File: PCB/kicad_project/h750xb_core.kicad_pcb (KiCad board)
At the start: 4 copper layers, 50 x 50 mm, 99 parts, among them Q1 Q_NMOS_GSD, SW1 SW_DPST, SW2 SW_DPST, U1 STM32H750XBHx, U2 TPS74801DRC, U3 TPS82130, U4 REF3020, U5 IS42S16160J, U6 IS42S16160J, U7 W25Q32JVZP, U8 W25Q32JVZP, Y1 32M, Y2 32.768k

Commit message: 123
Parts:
- moved D3 27.9 mm to (3.37, 92.2)
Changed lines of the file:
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@@
 	(footprint "Package_TO_SOT_SMD:SOT-23"
 		(layer "F.Cu")
-		(at -23.495 84.582)
+		(at 3.3704 92.248)
 		(descr "SOT, 3 Pin (https://www.jedec.org/system/files/docs/to-236h.pdf variant AB), generated with kicad-footprint-generator ipc_gullwing_generator.py")
 		(tags "SOT TO_SOT_SMD")
@@
 		(tags "resistor")
 		(property "Reference" "R8"
-			(at 0 -1.17 360)
+			(at 0 -1.17 0)
 			(layer "F.SilkS")
 			(hide yes)
@@
 		)
 		(property "Value" "4.99kΩ/12kΩ"
-			(at 0 1.17 360)
+			(at 0 1.17 0)
 			(layer "F.Fab")
 			(hide yes)
@@
 		)
 		(fp_text user "${REFERENCE}"
-			(at 0 0 360)
+			(at 0 0 0)
 			(layer "F.Fab")
 			(effects
@@
 		(tags "capacitor")
 		(property "Reference" "C42"
-			(at 0 -1.16 270)
+			(at 0 -1.16 -90)
 			(layer "F.SilkS")
 			(hide yes)
@@
 		)
 		(property "Value" "4.7uF"
-			(at 0 1.16 270)
+			(at 0 1.16 -90)
 			(layer "F.Fab")
 			(hide yes)
@@
 		)
 		(fp_text user "${REFERENCE}"
-			(at 0 0 270)
+			(at 0 0 -90)
 			(layer "F.Fab")
 			(effects

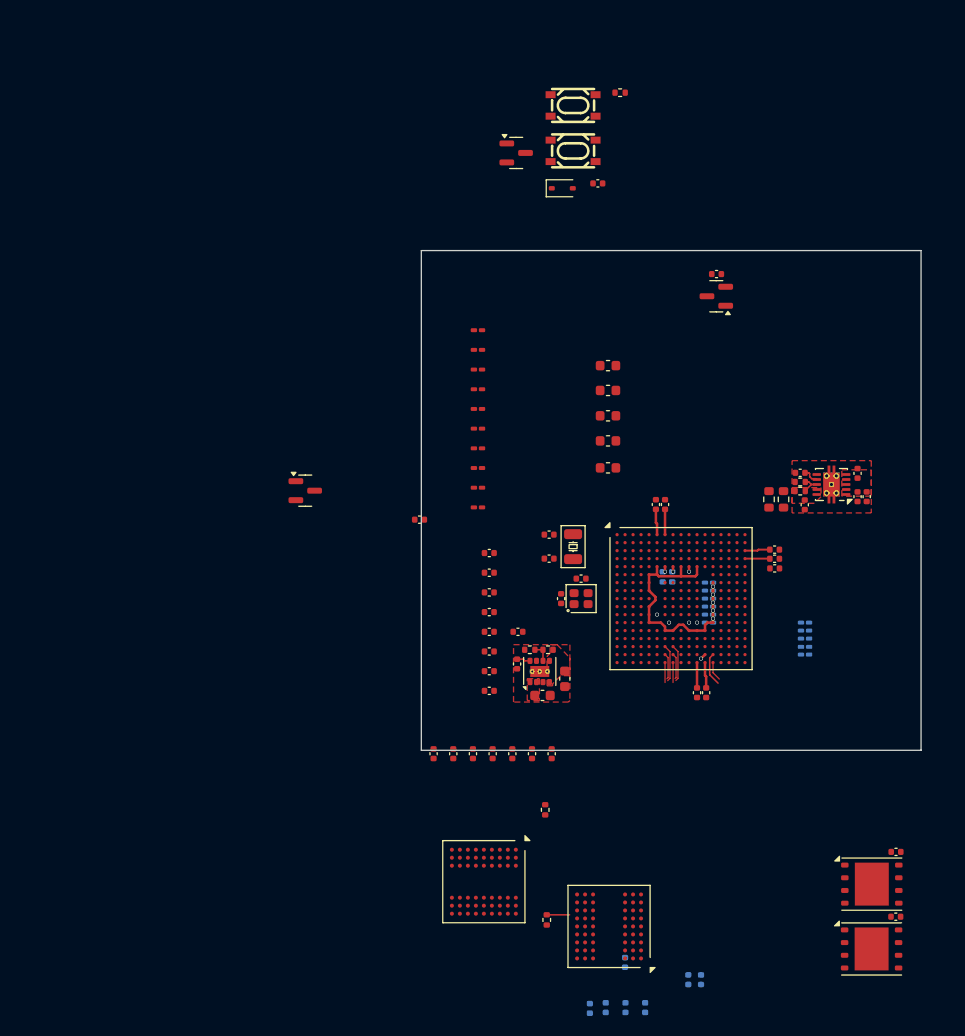
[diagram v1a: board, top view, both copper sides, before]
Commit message: 更新物料 删除16bit sdram*2 改为32bit sdram*1
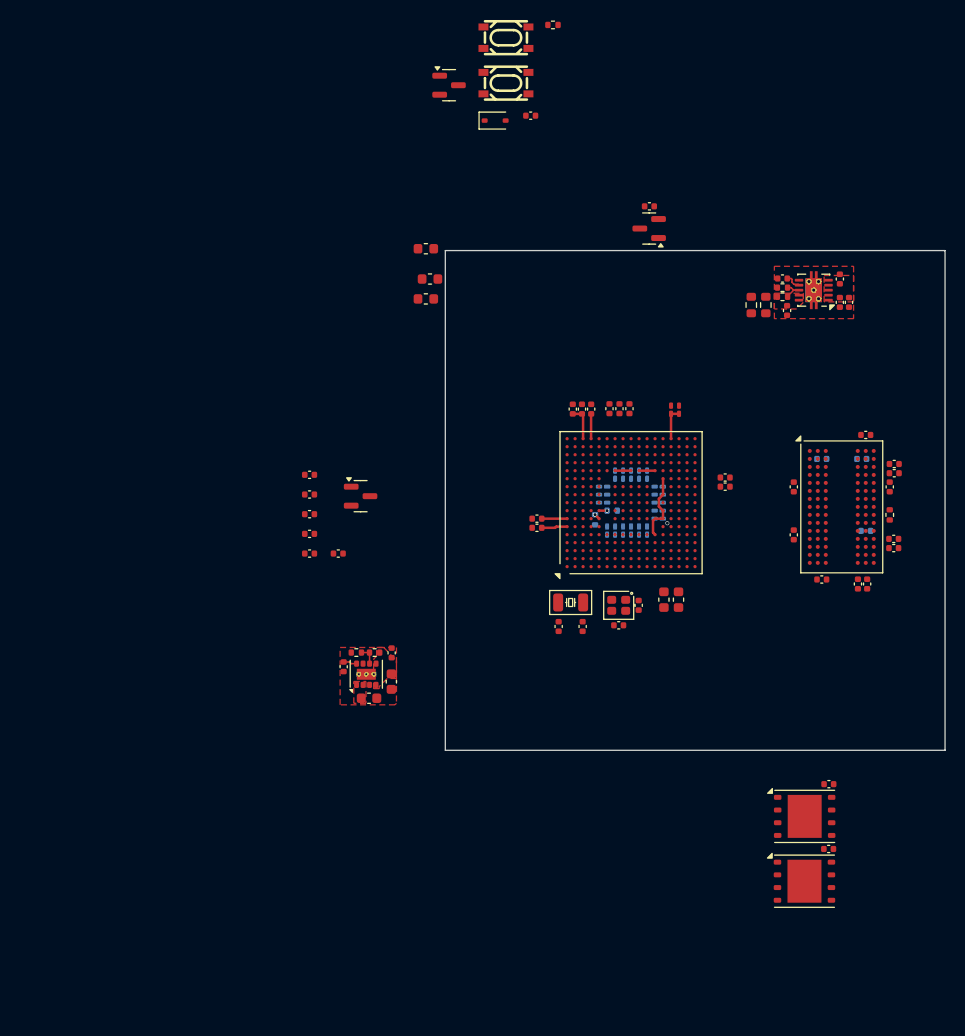
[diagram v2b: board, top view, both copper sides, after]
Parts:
- removed R12: 10K, Resistor_SMD:R_0402_1005Metric
- removed U5, U6: IS42S16160J, Package_BGA:Alliance_TFBGA-54_8x8mm_Layout9x9_P0.8mm
- added U9: ~, Package_BGA:BGA-90_8.0x13.0mm_Layout2x3x15_P0.8mm, F.Cu at (57.1, 93.9)
- C1, C10, C3, C4, C5, C6, C7, C8, C9: moved to B.Cu
- C16, C47, C48, C50, C53: moved to F.Cu
- R9: value 100kΩ -> 309kΩ
- moved C47 63.7 mm to (59.5, 86.7), turned to 180 degrees
- moved C48 57.6 mm to (61.9, 91.9), turned to -90 degrees
- moved C53 55.9 mm to (62.3, 90.5), turned to 180 degrees
- moved C52 54.9 mm to (59.1, 89.1), turned to 180 degrees
- moved C51 53.5 mm to (55.1, 89.1), turned to 180 degrees
- moved C49 53.4 mm to (59.5, 96.3), turned to 180 degrees
- moved R5 53.1 mm to (61.9, 94.7)
- moved C50 49.3 mm to (58.7, 101.6)
- moved C58 46.9 mm to (62.3, 98.0), turned to 180 degrees
- moved C60 46.6 mm to (59.6, 101.6), turned to 90 degrees
- moved C54 44.9 mm to (62.3, 89.6), turned to 180 degrees
- moved C56 43.8 mm to (62.3, 97.1), turned to 180 degrees
- moved C59 40.8 mm to (55.1, 101.1), turned to 180 degrees
- moved C55 37.4 mm to (52.3, 91.9), turned to 90 degrees
- moved C57 37.2 mm to (52.3, 96.7), turned to 90 degrees
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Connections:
- C27 pad 1: Net-(U1-VDD33_USB) -> +3V3
- C28 pad 1: Net-(U1-VDD33_USB) -> +3V3
- C29 pad 1: Net-(U1-VDD33_USB) -> +3V3
- U1 pad F17: Net-(U1-VDD33_USB) -> +3V3
- U1 pad G17: Net-(U1-VDD33_USB) -> +3V3
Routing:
- net +3V3: track 24.9 -> 13.4 mm, vias 5 -> 0
- net GND: track 4.25 -> 0.00 mm, vias 5 -> 0
- net /mcu/SDRAM_A6: track 3.71 -> 0.00 mm
- net /mcu/SDRAM_D16: track 3.34 -> 0.00 mm
- net /mcu/SDRAM_RAS: track 2.59 -> 0.00 mm
- net /mcu/SDRAM_A10: track 2.57 -> 0.00 mm
- net /mcu/VCAP: track 7.56 -> 5.02 mm
- net /mcu/SDRAM_CS#: track 2.29 -> 0.00 mm
- net unconnected-(U1-PJ4-PadU7): track 2.00 -> 0.00 mm
- net /mcu/SDRAM_A11: track 2.00 -> 0.00 mm
- net unconnected-(U1-PH7-PadU13): track 1.91 -> 0.00 mm
- net /mcu/VDDLDO: track 8.16 -> 6.36 mm
- net unconnected-(U1-PJ13-PadE10): track 0.51 -> 0.00 mm, vias 1 -> 0
- net unconnected-(U1-PJ0-PadN6): vias 0 -> 1

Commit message: MCU部分扇出，SDRAM走线ing
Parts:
- C22, C23, C24: moved to B.Cu
- C49, C51, C52, R2: moved to F.Cu
- moved FB2 45.7 mm to (43.2, 104.3), turned to -90 degrees
- moved U8 44.5 mm to (21.3, 100.4)
- moved U7 44.1 mm to (21.3, 94.5)
- moved C64 42.5 mm to (25.2, 98.5), turned to -90 degrees
- moved C63 42.1 mm to (25.2, 92.6), turned to -90 degrees
- moved C23 37.6 mm to (40.2, 102.2)
- moved C24 37.0 mm to (40.2, 101.3)
- moved C22 35.9 mm to (37.8, 102.2), turned to -90 degrees
- moved R2 6.13 mm to (28.0, 94.2), turned to 180 degrees
- moved C51 4.94 mm to (50.2, 89.8), turned to 90 degrees
- moved C65 2.75 mm to (30.2, 103.5), turned to 180 degrees
- moved C66 2.75 mm to (32.6, 103.5), turned to 0 degrees
- moved Y2 2.52 mm to (31.4, 105.5)
- moved R1 2.22 mm to (34.6, 95.4), turned to 0 degrees
- moved C53 2.12 mm to (60.2, 90.9)
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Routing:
- net /mcu/SDRAM_DQM2: track 0.00 -> 35.1 mm, vias 0 -> 1
- net +3V3: track 13.4 -> 47.7 mm, vias 0 -> 18
- net /mcu/SDRAM_DQM1: track 0.00 -> 33.2 mm, vias 0 -> 1
- net /mcu/SDRAM_D29: track 0.00 -> 33.0 mm, vias 0 -> 1
- net /mcu/SDRAM_DQM3: track 0.00 -> 32.1 mm, vias 0 -> 1
- net /mcu/SDRAM_CAS: track 0.00 -> 31.8 mm, vias 0 -> 1
- net /mcu/SDRAM_A0: track 0.00 -> 30.8 mm, vias 0 -> 1
- net /mcu/SDRAM_DQM0: track 0.00 -> 29.9 mm, vias 0 -> 2
- net /mcu/SDRAM_D24: track 0.00 -> 28.8 mm, vias 0 -> 1
- net /mcu/SDRAM_D28: track 0.00 -> 28.6 mm, vias 0 -> 1
- net /mcu/SDRAM_A1: track 0.00 -> 28.3 mm, vias 0 -> 1
- net /mcu/SDRAM_D30: track 0.00 -> 27.1 mm, vias 0 -> 2
- net /mcu/SDRAM_D26: track 0.00 -> 26.8 mm, vias 0 -> 1
- net /mcu/SDRAM_D2: track 0.00 -> 26.7 mm, vias 0 -> 2
- net /mcu/SDRAM_D27: track 0.00 -> 26.6 mm, vias 0 -> 1
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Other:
- copper layers 4 -> 6

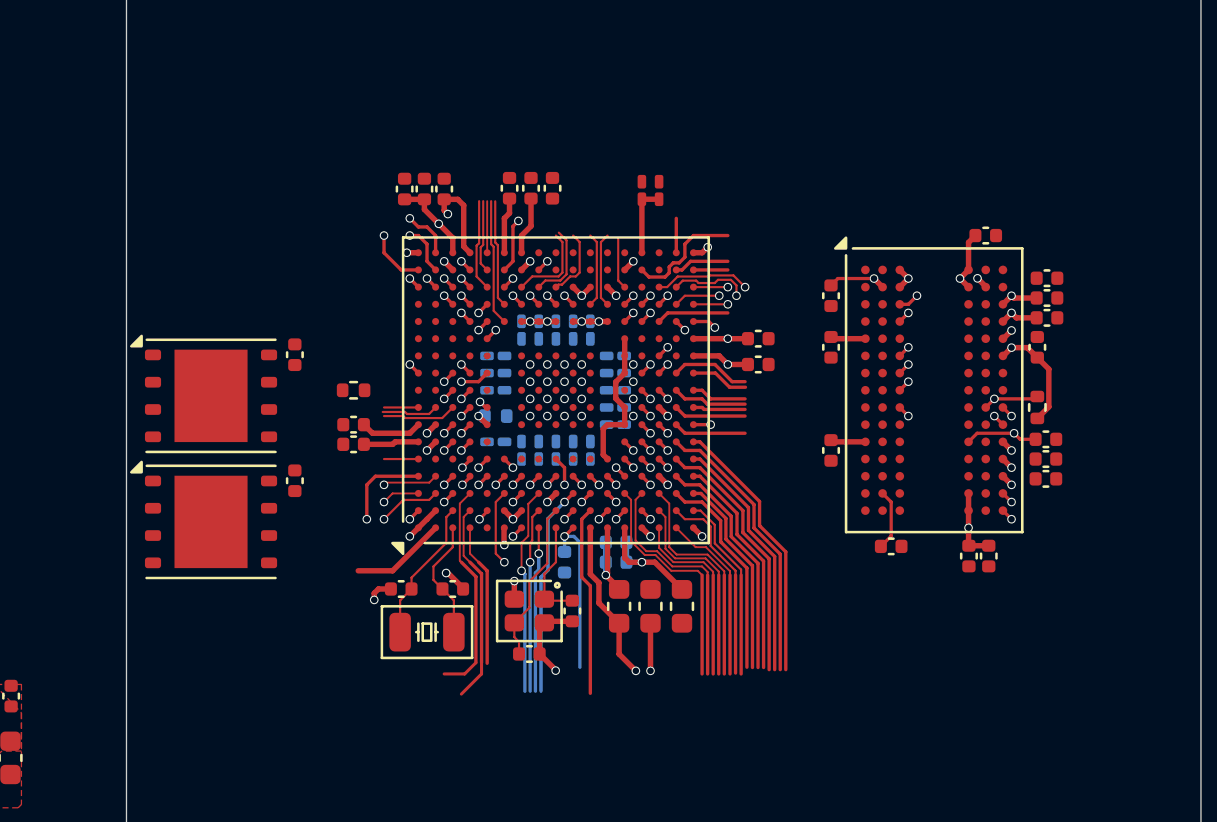
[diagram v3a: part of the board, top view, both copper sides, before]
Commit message: 绕走SDRAM走线。。因复杂度太高，放弃做等长 目前差最后几根数据线，可视情况交换线序
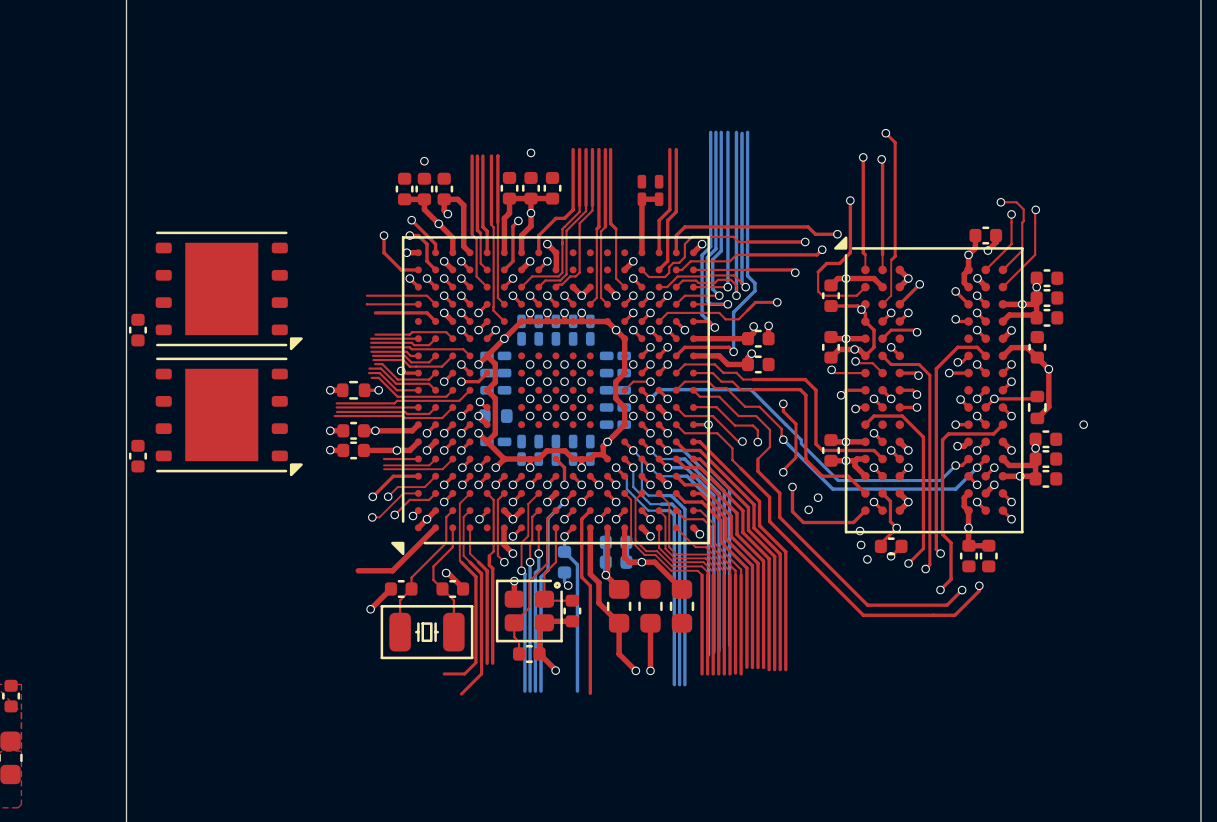
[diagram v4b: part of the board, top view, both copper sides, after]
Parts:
- moved U8 10.9 mm to (21.8, 89.5), turned to 180 degrees
- moved C64 10.1 mm to (17.9, 91.4), turned to 90 degrees
- moved C63 8.69 mm to (17.9, 97.3), turned to 90 degrees
- moved U7 1.02 mm to (21.8, 95.4), turned to 180 degrees
- moved C31 0.29 mm to (28.0, 96.1)
- moved C32 0.29 mm to (28.0, 97.0)
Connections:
- U9 pad A1: /mcu/SDRAM_D26 -> /mcu/SDRAM_D27
- U9 pad A8: /mcu/SDRAM_D23 -> /mcu/SDRAM_D21
- U9 pad A9: /mcu/SDRAM_D21 -> /mcu/SDRAM_D23
- U9 pad B1: /mcu/SDRAM_D28 -> /mcu/SDRAM_D25
- U9 pad B9: /mcu/SDRAM_D19 -> /mcu/SDRAM_D22
- U9 pad C2: /mcu/SDRAM_D27 -> /mcu/SDRAM_D26
- U9 pad C3: /mcu/SDRAM_D25 -> /mcu/SDRAM_D29
- U9 pad C7: /mcu/SDRAM_D22 -> /mcu/SDRAM_D20
- U9 pad C8: /mcu/SDRAM_D20 -> /mcu/SDRAM_D19
- U9 pad D2: /mcu/SDRAM_D29 -> /mcu/SDRAM_D31
- U9 pad E2: /mcu/SDRAM_D31 -> /mcu/SDRAM_D28
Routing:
- net /mcu/SDRAM_RAS: track 3.93 -> 29.3 mm, vias 1 -> 2
- net /mcu/SDRAM_D0: track 5.45 -> 30.5 mm, vias 0 -> 3
- net /mcu/SDRAM_D2: track 26.7 -> 50.9 mm
- net +3V3: track 47.7 -> 71.3 mm, vias 18 -> 28
- net /mcu/SDRAM_D3: track 25.7 -> 49.1 mm, vias 1 -> 2
- net /mcu/SDRAM_D14: track 1.60 -> 24.5 mm, vias 0 -> 2
- net /mcu/SDRAM_D4: track 3.13 -> 25.1 mm, vias 1 -> 2
- net /mcu/SDRAM_CAS: track 31.8 -> 53.7 mm, vias 1 -> 3
- net /mcu/SDRAM_A0: track 30.8 -> 52.4 mm, vias 1 -> 2
- net /mcu/SDRAM_CS#: track 3.18 -> 23.5 mm
- net /mcu/SDRAM_D15: track 2.57 -> 22.2 mm, vias 0 -> 3
- net /mcu/SDRAM_DQM0: track 29.9 -> 49.2 mm
- net /mcu/SDRAM_D9: track 0.57 -> 19.6 mm, vias 1 -> 2
- net /mcu/SDRAM_A2: track 26.6 -> 45.2 mm, vias 1 -> 2
- net /mcu/SDRAM_A1: track 28.3 -> 46.5 mm, vias 1 -> 2
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
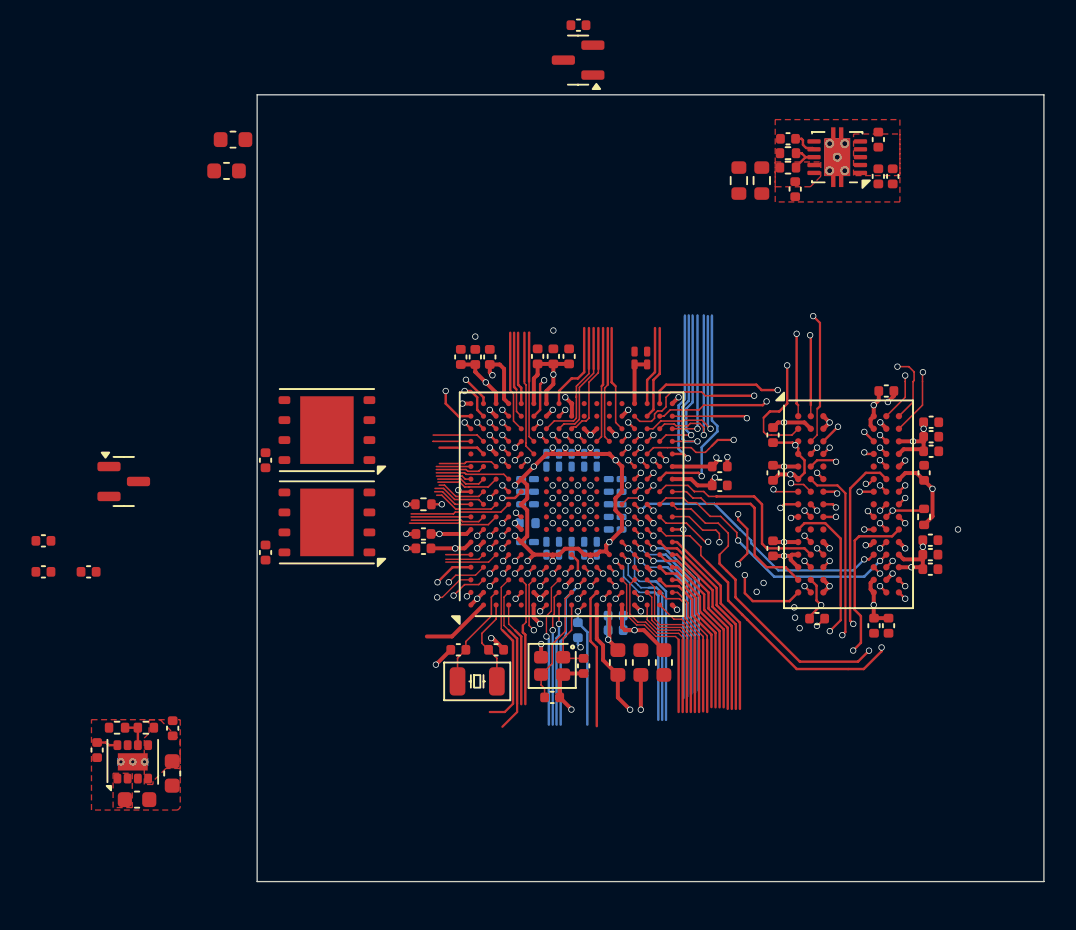
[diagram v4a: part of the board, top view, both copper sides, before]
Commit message: 完成了SDRAM和QSPI的走线，QSPI做了网络等长匹配（两根复用线未连接以用于准确计算线长）
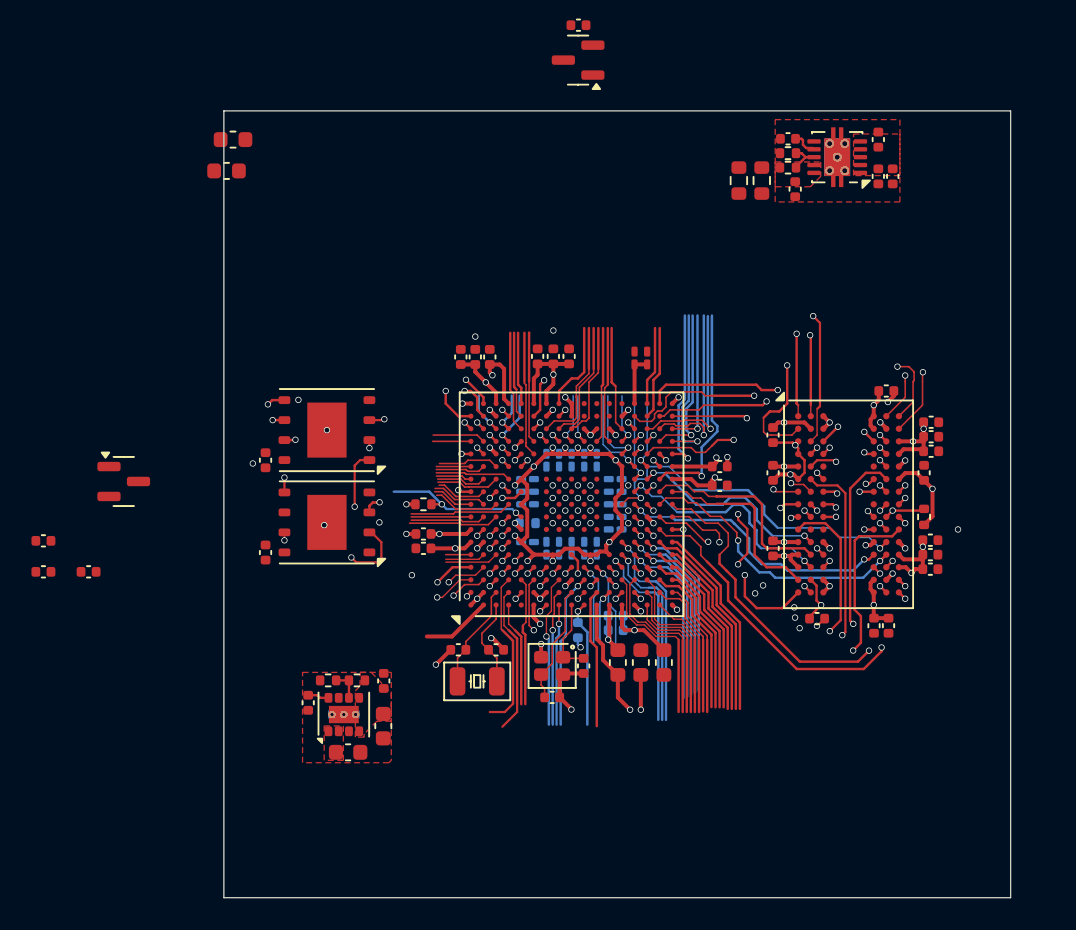
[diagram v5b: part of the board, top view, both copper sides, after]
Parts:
- moved C35 13.7 mm to (25.4, 105.5)
- moved C45 13.7 mm to (25.4, 108.3)
- moved R9 13.7 mm to (23.7, 105.4)
- moved C43 13.7 mm to (23.2, 110.0)
- moved C44 13.7 mm to (20.6, 106.9)
- moved R10 13.7 mm to (21.9, 105.4)
- moved U3 13.7 mm to (22.9, 107.6)
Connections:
- U1 pad E16: unconnected-(U1-PA12-PadE16) -> /mcu/USB_FS_D+
- U1 pad E17: unconnected-(U1-PA11-PadE17) -> /mcu/USB_FS_D-
- U9 pad L2: /mcu/SDRAM_D8 -> /mcu/SDRAM_D12
- U9 pad N2: /mcu/SDRAM_D12 -> /mcu/SDRAM_D8
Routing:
- net /mcu/SDRAM_D1: track 1.13 -> 39.1 mm
- net /mcu/QSPI1_IO1: track 0.00 -> 32.4 mm, vias 0 -> 2
- net /mcu/QSPI2_IO2: track 0.84 -> 32.7 mm, vias 1 -> 2
- net /mcu/QSPI_CS: track 2.97 -> 32.7 mm, vias 0 -> 2
- net /mcu/QSPI1_IO2: track 4.99 -> 32.5 mm, vias 1 -> 3
- net /mcu/QSPI2_IO3: track 6.08 -> 32.7 mm, vias 1 -> 2
- net /mcu/QSPI1_IO0: track 6.19 -> 32.4 mm, vias 1 -> 3
- net /mcu/QSPI1_IO3: track 10.5 -> 32.7 mm, vias 1 -> 2
- net /mcu/QSPI_CLK: track 10.9 -> 32.6 mm, vias 1 -> 3
- net /mcu/SDRAM_D7: track 1.93 -> 21.9 mm
- net /mcu/QSPI2_IO0: track 14.8 -> 32.9 mm, vias 1 -> 2
- net /mcu/QSPI2_IO1: track 15.9 -> 32.6 mm, vias 1 -> 3
- net /mcu/SDRAM_D8: track 1.13 -> 14.8 mm
- net /mcu/SDRAM_D12: track 1.13 -> 13.2 mm
- net /mcu/BOOT0: track 1.10 -> 9.42 mm
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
